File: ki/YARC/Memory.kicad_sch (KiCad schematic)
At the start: 16 parts, among them U14 74LS20, U18 AS6C6264, U20 74HC00, U21 74LS08, U22 74LS139, U23 74LS32, U24 AS6C6264, U25 74HC245, U26 74LS157, U27 AS6C6264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

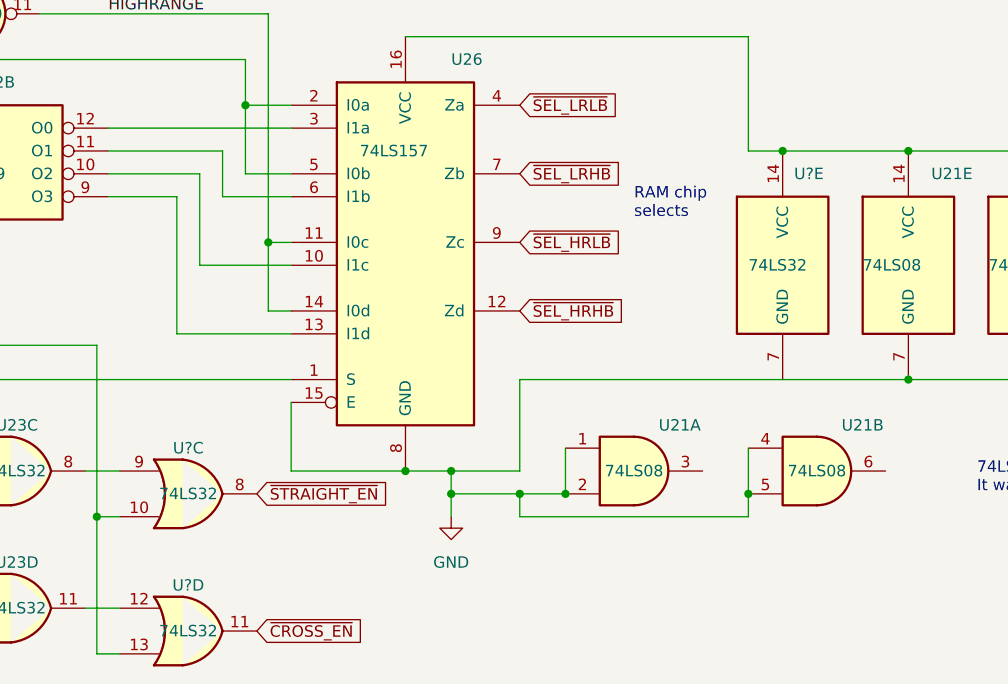
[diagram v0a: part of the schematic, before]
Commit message: Assign part labels (U-numbers) in KiCad and start adding them to Fritzing layouts
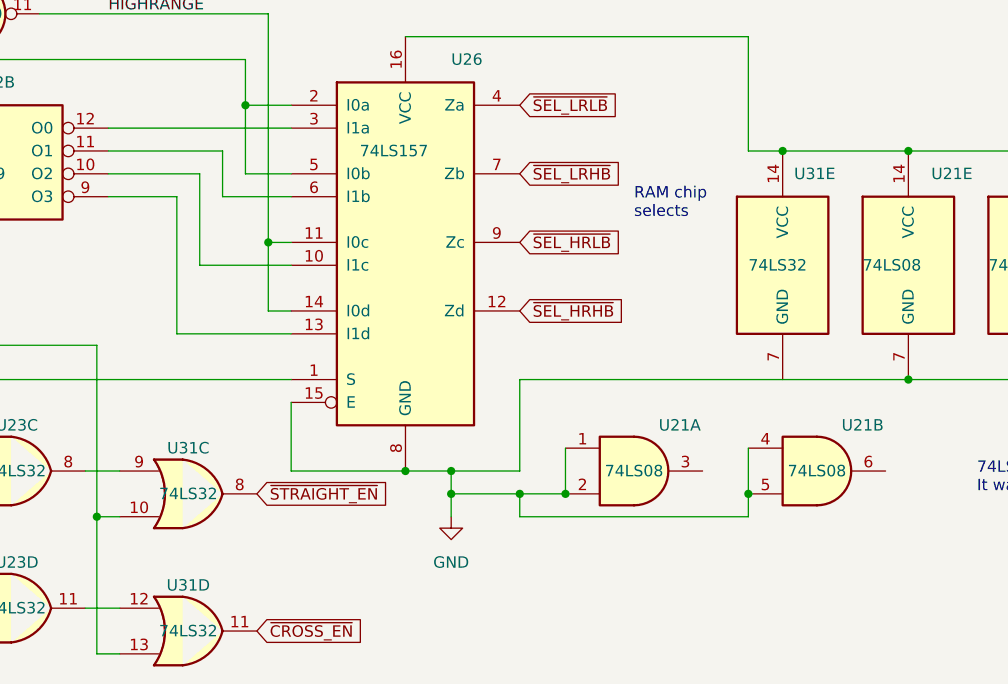
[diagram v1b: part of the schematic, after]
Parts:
- gave numbers to parts that had none: 1
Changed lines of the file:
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@@
   (symbol (lib_id "74xx:74LS32") (at 120.65 182.88 0) (unit 3)
     (in_bom yes) (on_board yes)
-    (property "Reference" "U?" (id 0) (at 120.65 177.8 0))
+    (property "Reference" "U31" (id 0) (at 120.65 177.8 0))
     (property "Value" "74LS32" (id 1) (at 120.65 182.88 0))
     (property "Footprint" "" (id 2) (at 120.65 182.88 0)
@@
   (symbol (lib_id "74xx:74LS32") (at 186.69 157.48 0) (unit 5)
     (in_bom yes) (on_board yes)
-    (property "Reference" "U?" (id 0) (at 187.96 147.32 0)
+    (property "Reference" "U31" (id 0) (at 187.96 147.32 0)
       (effects (font (size 1.27 1.27)) (justify left))
     )
@@
   (symbol (lib_id "74xx:74LS32") (at 120.65 198.12 0) (unit 4)
     (in_bom yes) (on_board yes)
-    (property "Reference" "U?" (id 0) (at 120.65 193.04 0))
+    (property "Reference" "U31" (id 0) (at 120.65 193.04 0))
     (property "Value" "74LS32" (id 1) (at 120.65 198.12 0))
     (property "Footprint" "" (id 2) (at 120.65 198.12 0)

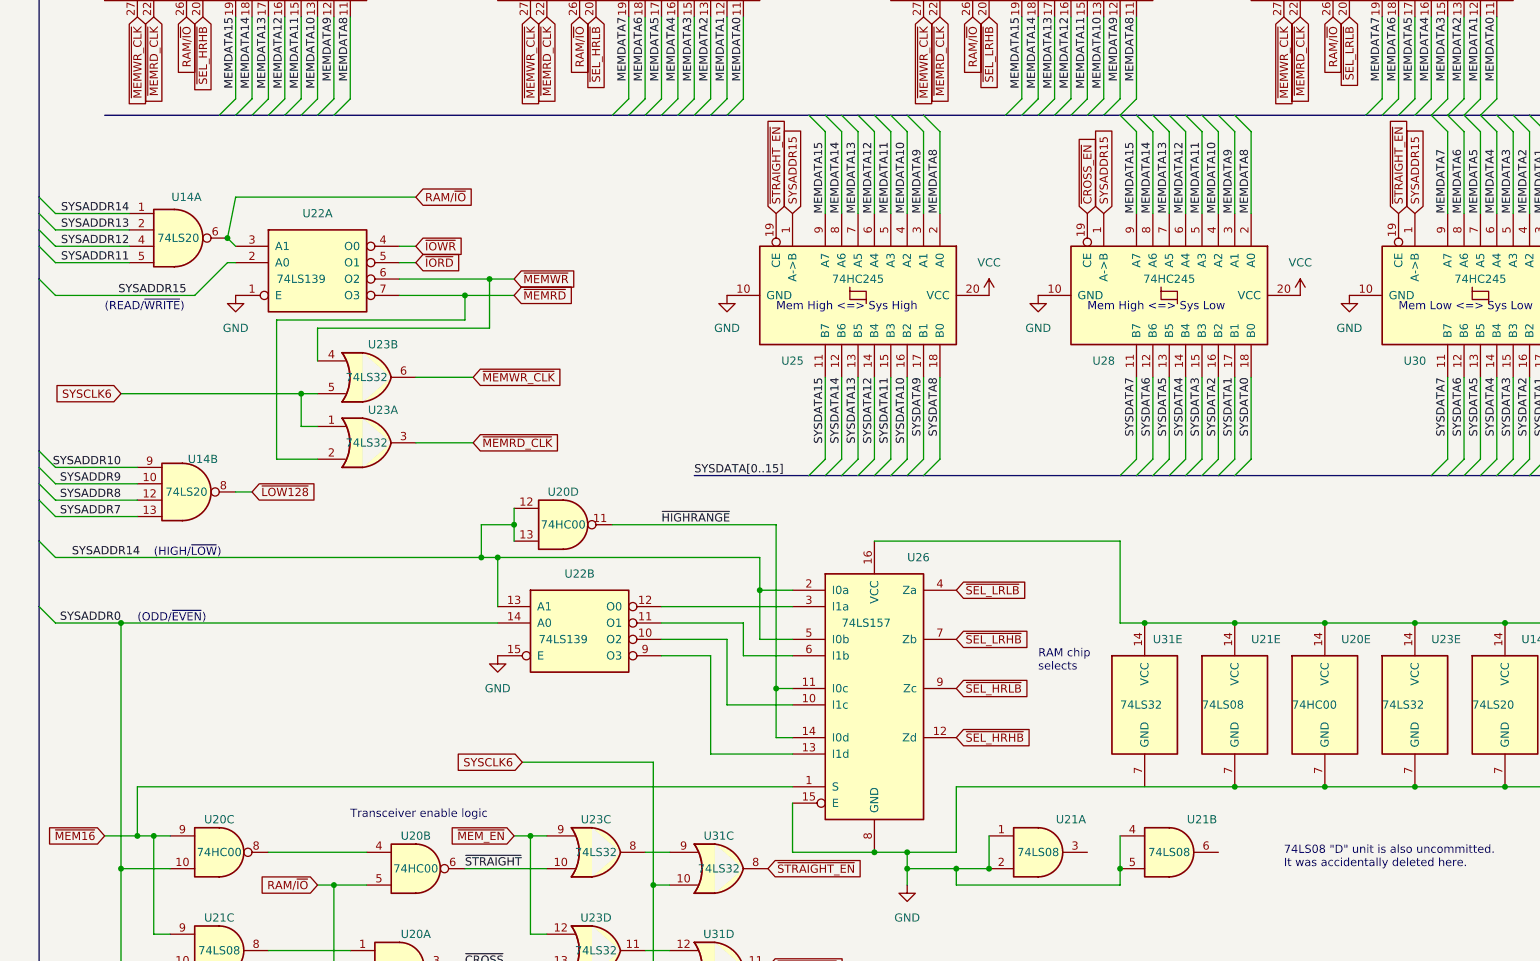
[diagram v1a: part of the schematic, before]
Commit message: Flags development and implement memory fix. Firmware not updated to match the memory fix.
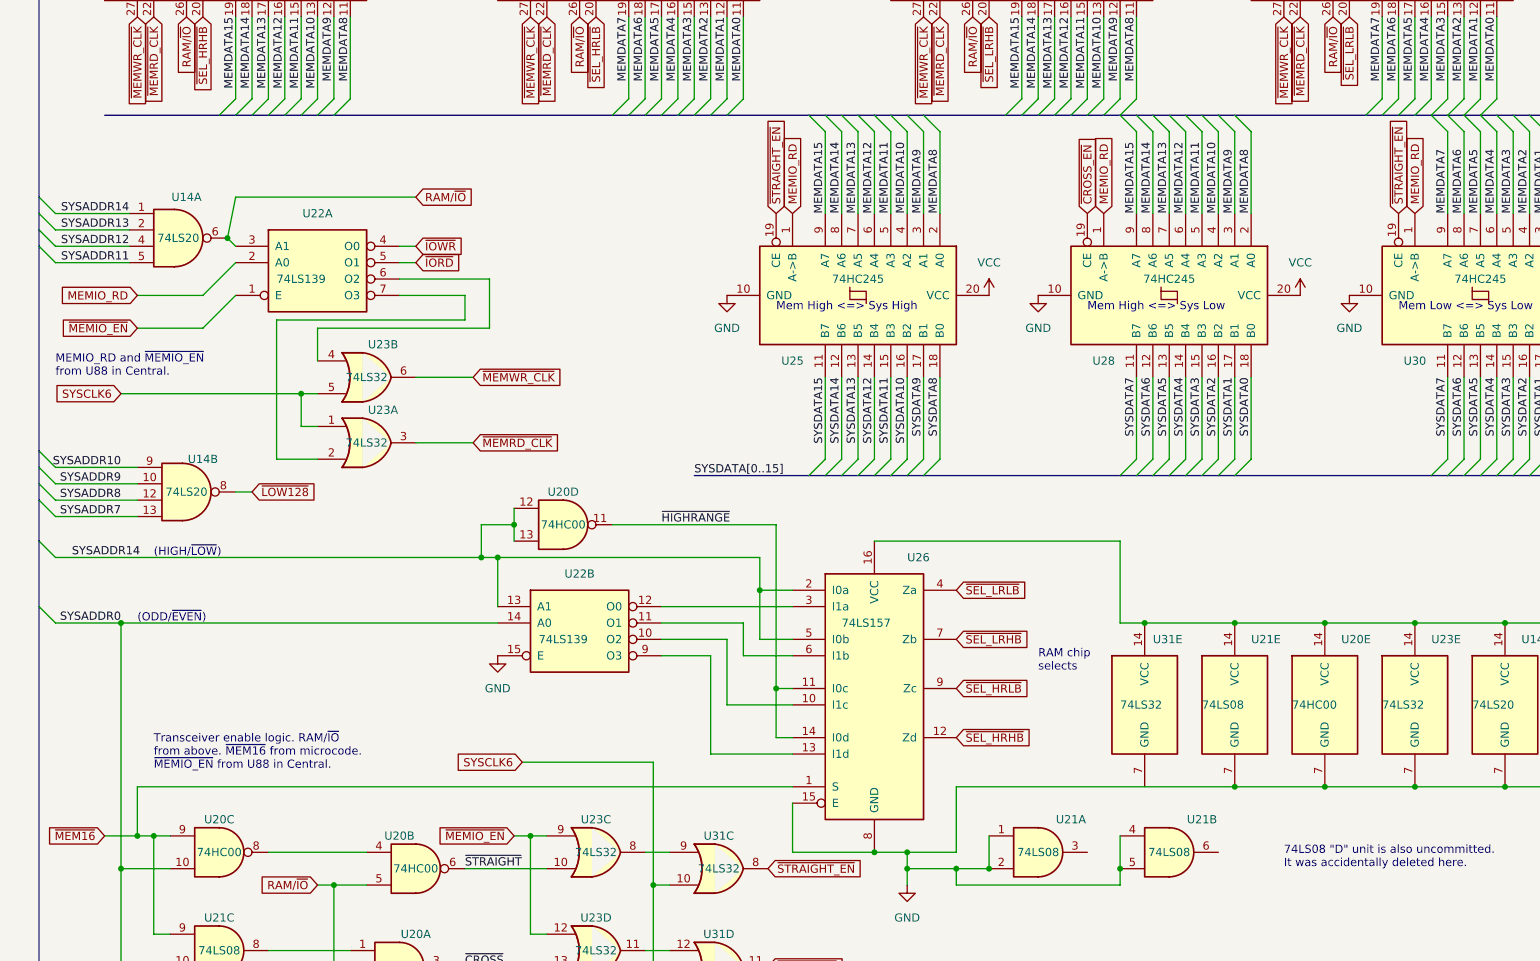
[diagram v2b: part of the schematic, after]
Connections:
- net GND: no longer U22.1 (E)
- net SYSADDR15 renamed MEMIO_RD
- net ~{MEMRD}: no longer names the net of U22.7 (O3), U23.2
- net ~{MEMWR}: no longer names the net of U22.6 (O2), U23.4
- net ~{MEM_EN} renamed ~{MEMIO_EN}
- net ~{MEMIO_EN}: now also U22.1 (E)
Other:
- note added: "MEMIO_RD and ~{MEMIO_EN} from U88 in Central."
- note added: "Transceiver enable logic. RAM/~{IO} from above. ~{MEM16} from microcode. ~{MEMIO_EN} from U88 in Central."
- note removed: "(READ/~{WRITE})"
- note removed: "Transceiver enable logic"

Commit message: New memory control logic passes a basic test. Firmware loops after reset running the test.
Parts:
- renumbered U31 to U23, U23 to U96
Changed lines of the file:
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@@
   (symbol (lib_id "74xx:74LS32") (at 101.6 180.34 0) (unit 3)
     (in_bom yes) (on_board yes)
-    (property "Reference" "U23" (id 0) (at 101.6 175.26 0))
+    (property "Reference" "U96" (id 0) (at 101.6 175.26 0))
     (property "Value" "74LS32" (id 1) (at 101.6 180.34 0))
     (property "Footprint" "" (id 2) (at 101.6 180.34 0)
@@
   (symbol (lib_id "74xx:74LS32") (at 120.65 182.88 0) (unit 3)
     (in_bom yes) (on_board yes)
-    (property "Reference" "U31" (id 0) (at 120.65 177.8 0))
+    (property "Reference" "U23" (id 0) (at 120.65 177.8 0))
     (property "Value" "74LS32" (id 1) (at 120.65 182.88 0))
     (property "Footprint" "" (id 2) (at 120.65 182.88 0)
@@
   (symbol (lib_id "74xx:74LS32") (at 120.65 198.12 0) (unit 4)
     (in_bom yes) (on_board yes)
-    (property "Reference" "U31" (id 0) (at 120.65 193.04 0))
+    (property "Reference" "U23" (id 0) (at 120.65 193.04 0))
     (property "Value" "74LS32" (id 1) (at 120.65 198.12 0))
     (property "Footprint" "" (id 2) (at 120.65 198.12 0)
@@
   (symbol (lib_id "74xx:74LS32") (at 101.6 195.58 0) (unit 4)
     (in_bom yes) (on_board yes)
-    (property "Reference" "U23" (id 0) (at 101.6 190.5 0))
+    (property "Reference" "U96" (id 0) (at 101.6 190.5 0))
     (property "Value" "74LS32" (id 1) (at 101.6 195.58 0))
     (property "Footprint" "" (id 2) (at 101.6 195.58 0)

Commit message: Various corrections and minor improvements
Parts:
- renumbered U96 to U100
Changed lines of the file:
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@@
   (symbol (lib_id "74xx:74LS32") (at 101.6 180.34 0) (unit 3)
     (in_bom yes) (on_board yes)
-    (property "Reference" "U96" (id 0) (at 101.6 175.26 0))
+    (property "Reference" "U100" (id 0) (at 101.6 175.26 0))
     (property "Value" "74LS32" (id 1) (at 101.6 180.34 0))
     (property "Footprint" "" (id 2) (at 101.6 180.34 0)
@@
   (symbol (lib_id "74xx:74LS32") (at 101.6 195.58 0) (unit 4)
     (in_bom yes) (on_board yes)
-    (property "Reference" "U96" (id 0) (at 101.6 190.5 0))
+    (property "Reference" "U100" (id 0) (at 101.6 190.5 0))
     (property "Value" "74LS32" (id 1) (at 101.6 195.58 0))
     (property "Footprint" "" (id 2) (at 101.6 195.58 0)

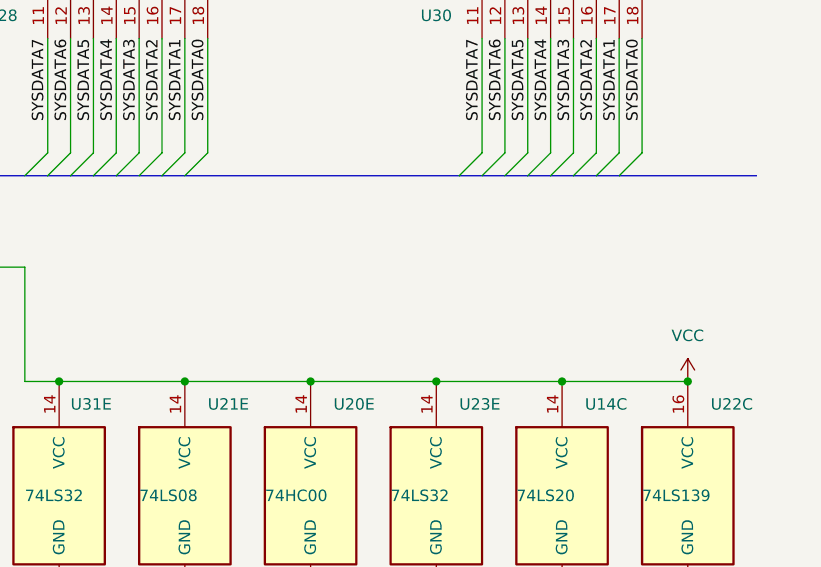
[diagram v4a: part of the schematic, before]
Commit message: Cleanups on the way to first execution - no significant functional changes
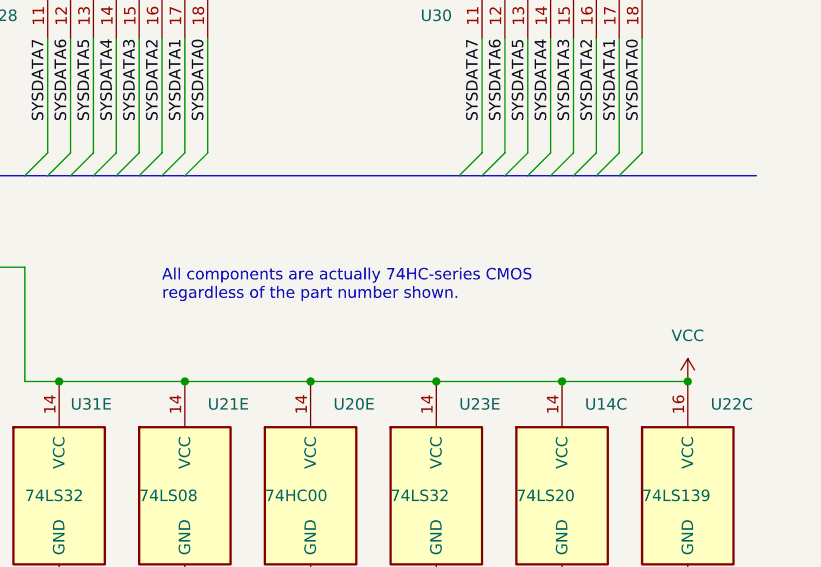
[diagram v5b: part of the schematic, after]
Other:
- note added: "All components are actually 74HC-series CMOS regardless of the part number shown."
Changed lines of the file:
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@@
+    (effects (font (size 1.27 1.27)) (justify left bottom))
+  )
+  (text "All components are actually 74HC-series CMOS\nregardless of the part number shown."
+    (at 198.12 135.89 0)
     (effects (font (size 1.27 1.27)) (justify left bottom))
   )

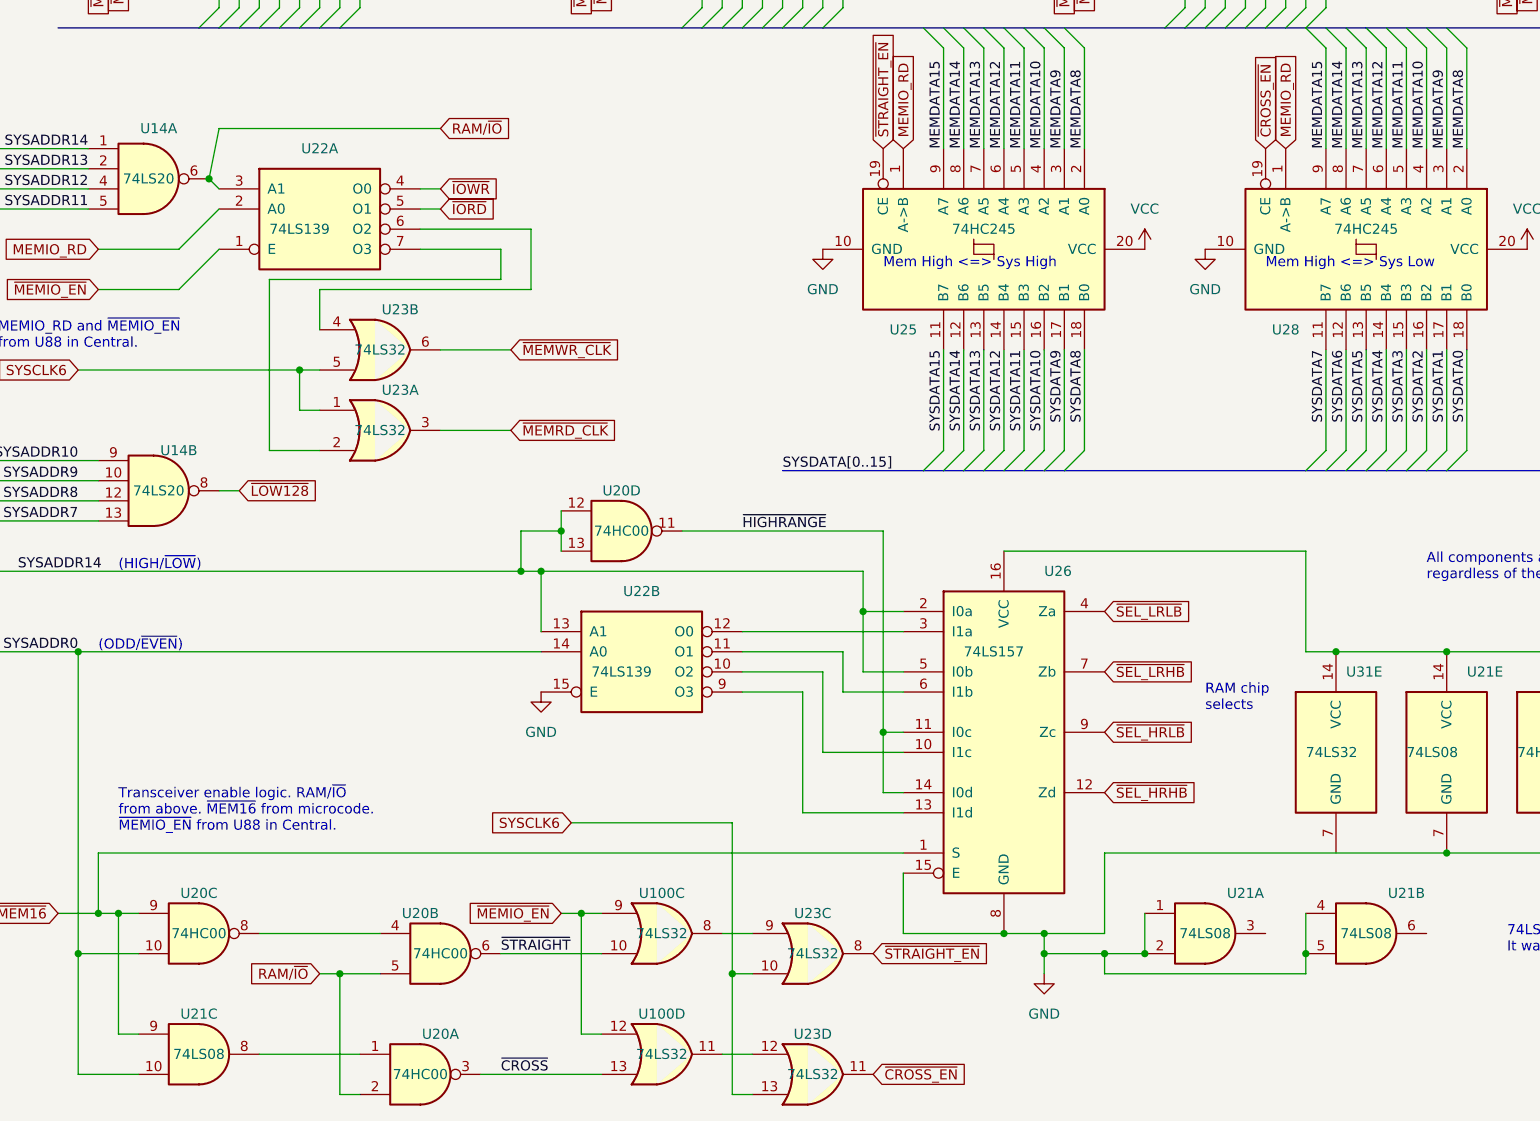
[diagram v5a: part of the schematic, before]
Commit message: Convert schematic to KiCad 7
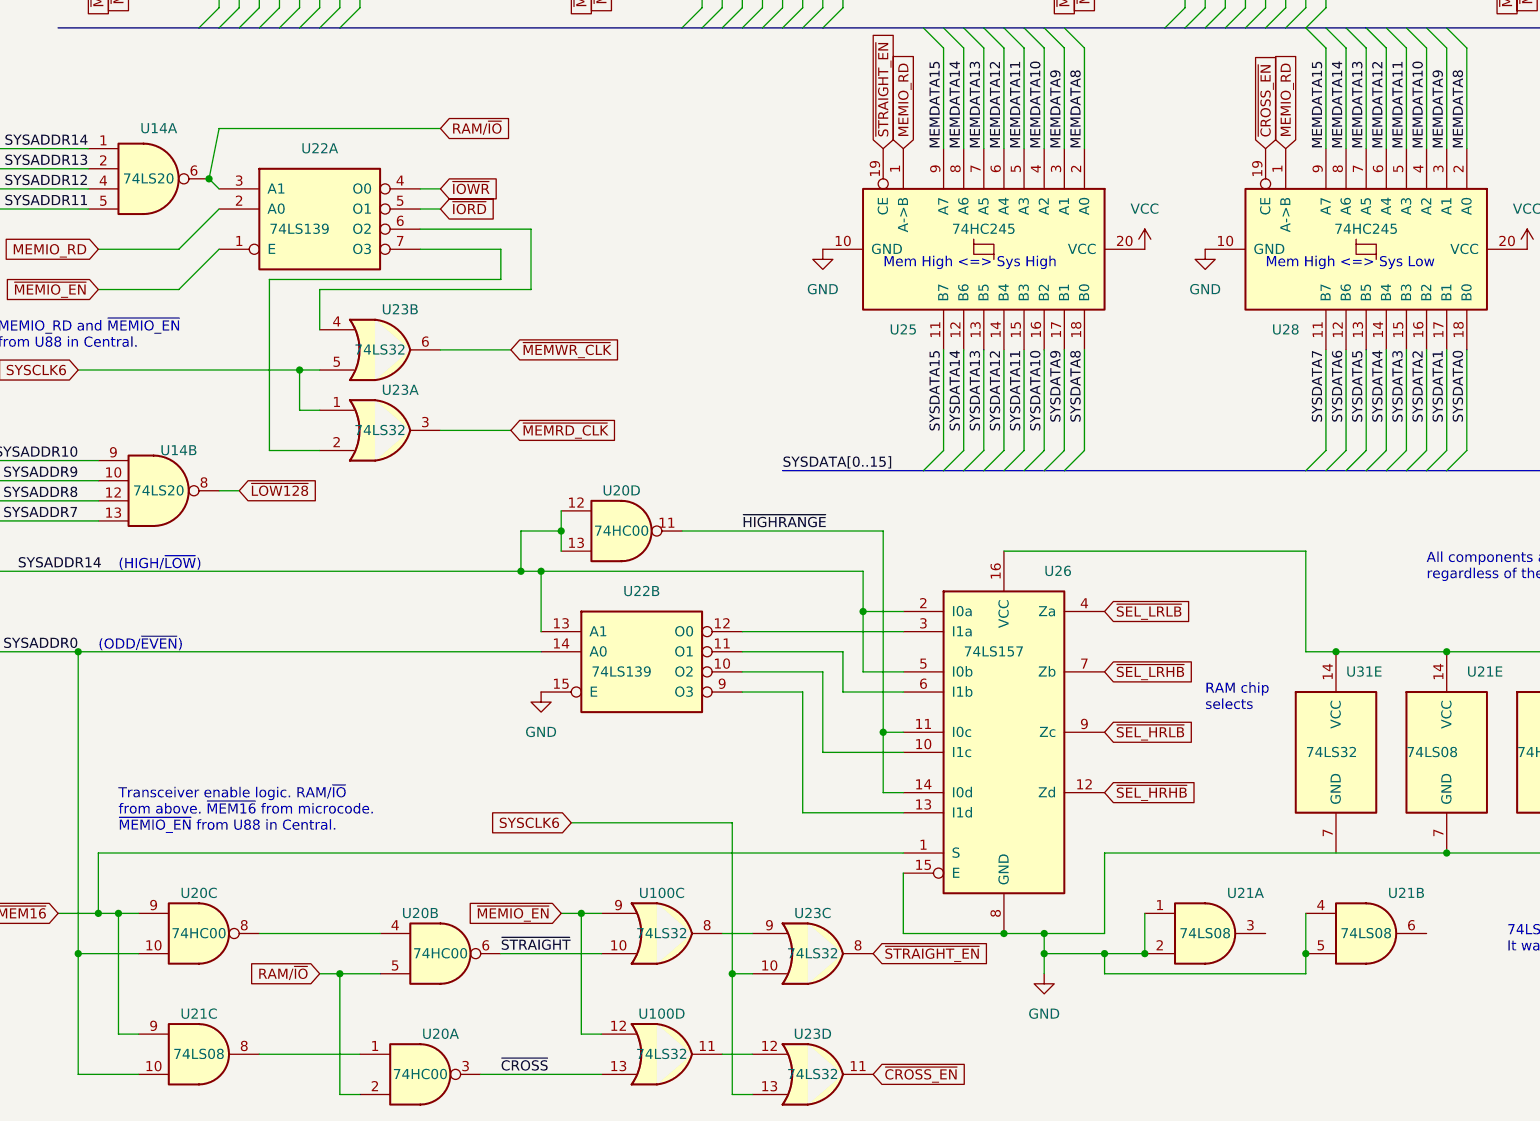
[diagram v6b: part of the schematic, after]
